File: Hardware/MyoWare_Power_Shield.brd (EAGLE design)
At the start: 52.1 x 20.7 mm, 14 parts

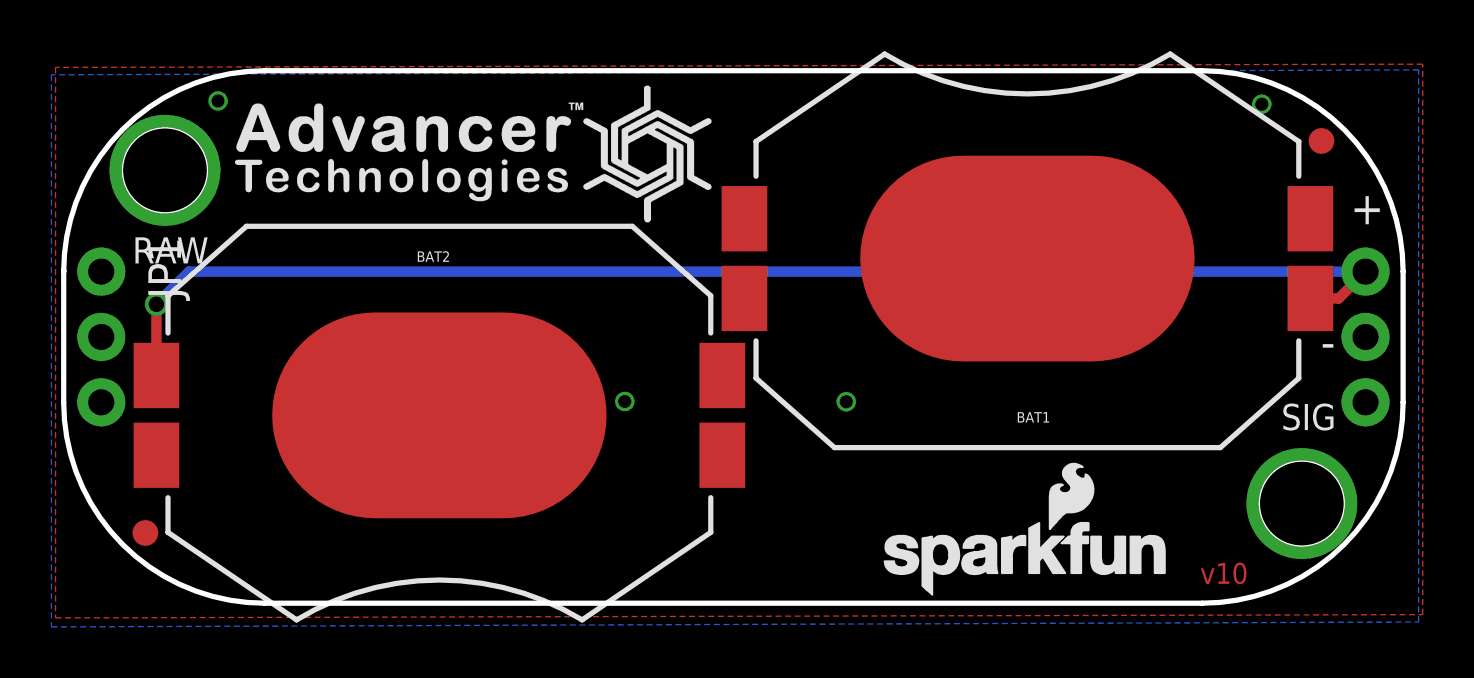
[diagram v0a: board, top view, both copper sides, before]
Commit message: Expanded dimensions to nearest 0.01" grid
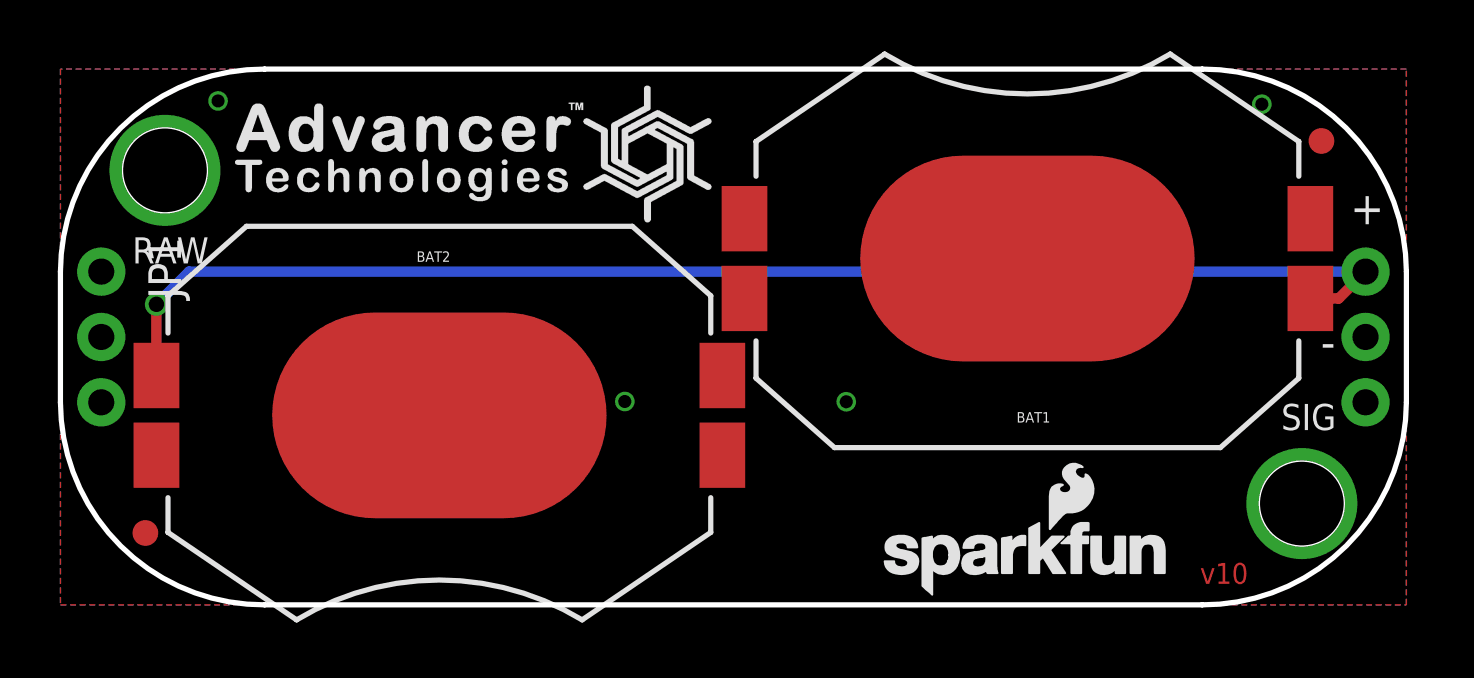
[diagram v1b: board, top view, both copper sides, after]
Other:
- board size 52.1 x 20.7 mm -> 52.3 x 20.8 mm
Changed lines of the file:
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@@
 <setting verticaltext="up"/>
 </settings>
-<grid distance="0.05" unitdist="inch" unit="inch" style="lines" multiple="1" display="yes" altdistance="0.005" altunitdist="inch" altunit="inch"/>
+<grid distance="0.01" unitdist="inch" unit="inch" style="lines" multiple="1" display="yes" altdistance="0.005" altunitdist="inch" altunit="inch"/>
 <layers>
 <layer number="1" name="Top" color="4" fill="1" visible="yes" active="yes"/>
@@
 <layer number="45" name="Holes" color="7" fill="1" visible="yes" active="yes"/>
 <layer number="46" name="Milling" color="3" fill="1" visible="no" active="yes"/>
-<layer number="47" name="Measures" color="7" fill="1" visible="no" active="yes"/>
+<layer number="47" name="Measures" color="7" fill="1" visible="yes" active="yes"/>
 <layer number="48" name="Document" color="7" fill="1" visible="no" active="yes"/>
 <layer number="49" name="Reference" color="3" fill="1" visible="no" active="yes"/>
@@
 <text x="23.4315" y="-3.1115" size="1.016" layer="21" ratio="17" rot="R180" align="center-left">SIG</text>
 <text x="23.39975" y="-0.1905" size="1.27" layer="21" ratio="17" rot="R180" align="center-left">-</text>
-<wire x1="-18.2245" y1="-10.3505" x2="18.2245" y2="-10.3505" width="0.2032" layer="20"/>
+<wire x1="-18.2245" y1="-10.414" x2="18.2245" y2="-10.414" width="0.2032" layer="20"/>
 <text x="-23.368" y="3.3655" size="1.016" layer="21" ratio="17" align="center-left">RAW</text>
-<wire x1="-26.035" y1="-2.54" x2="-26.035" y2="2.54" width="0.2032" layer="20"/>
-<wire x1="-26.035" y1="2.54" x2="-26.035" y2="2.6035" width="0.2032" layer="20"/>
-<wire x1="-18.2245" y1="10.3505" x2="-26.035" y2="2.54" width="0.2032" layer="20" curve="90"/>
-<wire x1="-26.035" y1="-2.54" x2="-18.2245" y2="-10.3505" width="0.2032" layer="20" curve="90"/>
-<wire x1="26.035" y1="2.54" x2="26.035" y2="-2.54" width="0.2032" layer="20"/>
-<wire x1="18.2245" y1="-10.3505" x2="26.035" y2="-2.54" width="0.2032" layer="20" curve="90"/>
-<wire x1="26.035" y1="2.54" x2="18.2245" y2="10.3505" width="0.2032" layer="20" curve="90"/>
+<wire x1="-26.162" y1="-2.54" x2="-26.162" y2="2.54" width="0.2032" layer="20"/>
+<wire x1="-18.2245" y1="10.414" x2="-26.162" y2="2.54" width="0.2032" layer="20" curve="90"/>
+<wire x1="-26.162" y1="-2.54" x2="-18.2245" y2="-10.414" width="0.2032" layer="20" curve="90"/>
+<wire x1="26.162" y1="2.54" x2="26.162" y2="-2.54" width="0.2032" layer="20"/>
+<wire x1="18.2245" y1="-10.414" x2="26.162" y2="-2.54" width="0.2032" layer="20" curve="90"/>
+<wire x1="26.162" y1="2.54" x2="18.2245" y2="10.414" width="0.2032" layer="20" curve="90"/>
 <text x="0" y="-7.14375" size="1.27" layer="22" font="vector" ratio="20" rot="MR0" align="center">Power Shield</text>
-<wire x1="-18.2245" y1="10.3505" x2="18.2245" y2="10.3505" width="0.2032" layer="20"/>
+<wire x1="-18.2245" y1="10.414" x2="18.2245" y2="10.414" width="0.2032" layer="20"/>
 <text x="0" y="8.09625" size="1.27" layer="22" font="vector" ratio="15" rot="MR0" align="center">Insert batteries (-) side to PCB</text>
 <text x="-1.825" y="-32.453" size="1.778" layer="51" font="vector">Brian E Kaminski of Advancer Technologies</text>
 <text x="-20.875" y="-34.993" size="1.778" layer="51" font="vector">Revised by: Brent Wilkins</text>
 <text x="18.1405" y="-9.598" size="0.8128" layer="1" font="vector" ratio="20">v10</text>
-<dimension x1="-22.098" y1="6.477" x2="22.098" y2="-6.477" x3="-30.48" y3="0" textsize="1.778" layer="47" dtype="vertical" unit="inch"/>
-<dimension x1="-18.2245" y1="-10.3505" x2="-15.031465625" y2="10.344659375" x3="-35.012628125" y3="-0.00291875" textsize="1.778" layer="47" dtype="vertical" unit="inch"/>
-<dimension x1="-22.098" y1="6.477" x2="22.098" y2="-6.477" x3="0" y3="14.683740625" textsize="1.778" layer="47" dtype="horizontal" unit="inch"/>
-<dimension x1="26.035" y1="2.54" x2="-26.035" y2="2.54" x3="0" y3="18.975325" textsize="1.778" layer="47" unit="inch"/>
-<dimension x1="22.098" y1="-6.477" x2="26.63825" y2="-11.08075" x3="28.953459375" y3="-11.0799875" textsize="1.778" layer="47" dtype="leader" unit="inch"/>
-<text x="28.991053125" y="-11.0878625" size="1.27" layer="47" font="vector">0.13" diameter typical</text>
+<dimension x1="-22.098" y1="6.477" x2="22.098" y2="-6.477" x3="-28.194" y3="0" textsize="1.778" textratio="15" layer="47" dtype="vertical" unit="inch"/>
+<dimension x1="-22.098" y1="6.477" x2="22.098" y2="-6.477" x3="0" y3="13.921740625" textsize="1.778" textratio="15" layer="47" dtype="horizontal" unit="inch"/>
+<dimension x1="22.098" y1="-6.477" x2="26.63825" y2="-11.08075" x3="28.953459375" y3="-11.0799875" textsize="1.778" textratio="15" layer="47" dtype="leader" unit="inch"/>
+<text x="28.991053125" y="-11.0878625" size="1.27" layer="47" font="vector" ratio="15">0.13" diameter typical</text>
 <text x="0" y="23.58516875" size="1.778" layer="47" font="vector" ratio="15" align="center">All units in inches</text>
 <text x="23.3242625" y="0.001940625" size="1.016" layer="22" font="vector" ratio="15" rot="MR0" align="center-left">GND</text>
@@
 <text x="-23.3278375" y="2.541353125" size="1.016" layer="22" font="vector" ratio="15" rot="MR0" align="center-right">RAW</text>
 <text x="-23.2778375" y="-2.5418875" size="1.016" layer="22" font="vector" ratio="15" rot="MR0" align="center-right">GND</text>
+<dimension x1="-18.2245" y1="10.414" x2="-18.034" y2="-10.414" x3="-32.766" y3="0" textsize="1.778" textratio="15" layer="47" dtype="vertical" unit="inch"/>
+<dimension x1="-26.162" y1="2.54" x2="26.162" y2="2.286" x3="0" y3="18.542" textsize="1.778" textratio="15" layer="47" dtype="horizontal" unit="inch"/>
 </plain>
 <attributes>
@@
 <signal name="GND" airwireshidden="yes">
 <polygon width="0.2032" layer="1">
-<vertex x="-26.3525" y="-10.922"/>
-<vertex x="26.797" y="-10.795"/>
-<vertex x="26.797" y="10.6045"/>
-<vertex x="-26.3525" y="10.4775"/>
+<vertex x="-26.162" y="-10.414"/>
+<vertex x="26.162" y="-10.414"/>
+<vertex x="26.162" y="10.414"/>
+<vertex x="-26.162" y="10.414"/>
 </polygon>
 <polygon width="0.2032" layer="16">
-<vertex x="-26.51125" y="-11.27125"/>
-<vertex x="26.63825" y="-11.08075"/>
-<vertex x="26.63825" y="10.38225"/>
-<vertex x="-26.51125" y="10.19175"/>
+<vertex x="-26.162" y="-10.414"/>
+<vertex x="26.162" y="-10.414"/>
+<vertex x="26.162" y="10.414"/>
+<vertex x="-26.162" y="10.414"/>
 </polygon>
 <contactref element="JP2" pad="2"/>
